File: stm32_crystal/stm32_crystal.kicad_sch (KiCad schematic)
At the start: 22 parts, among them U1 STM32F103C6Tx, U2 CR2032-BS-5-1, Y1 Crystal_Small, Y2 8Mhz

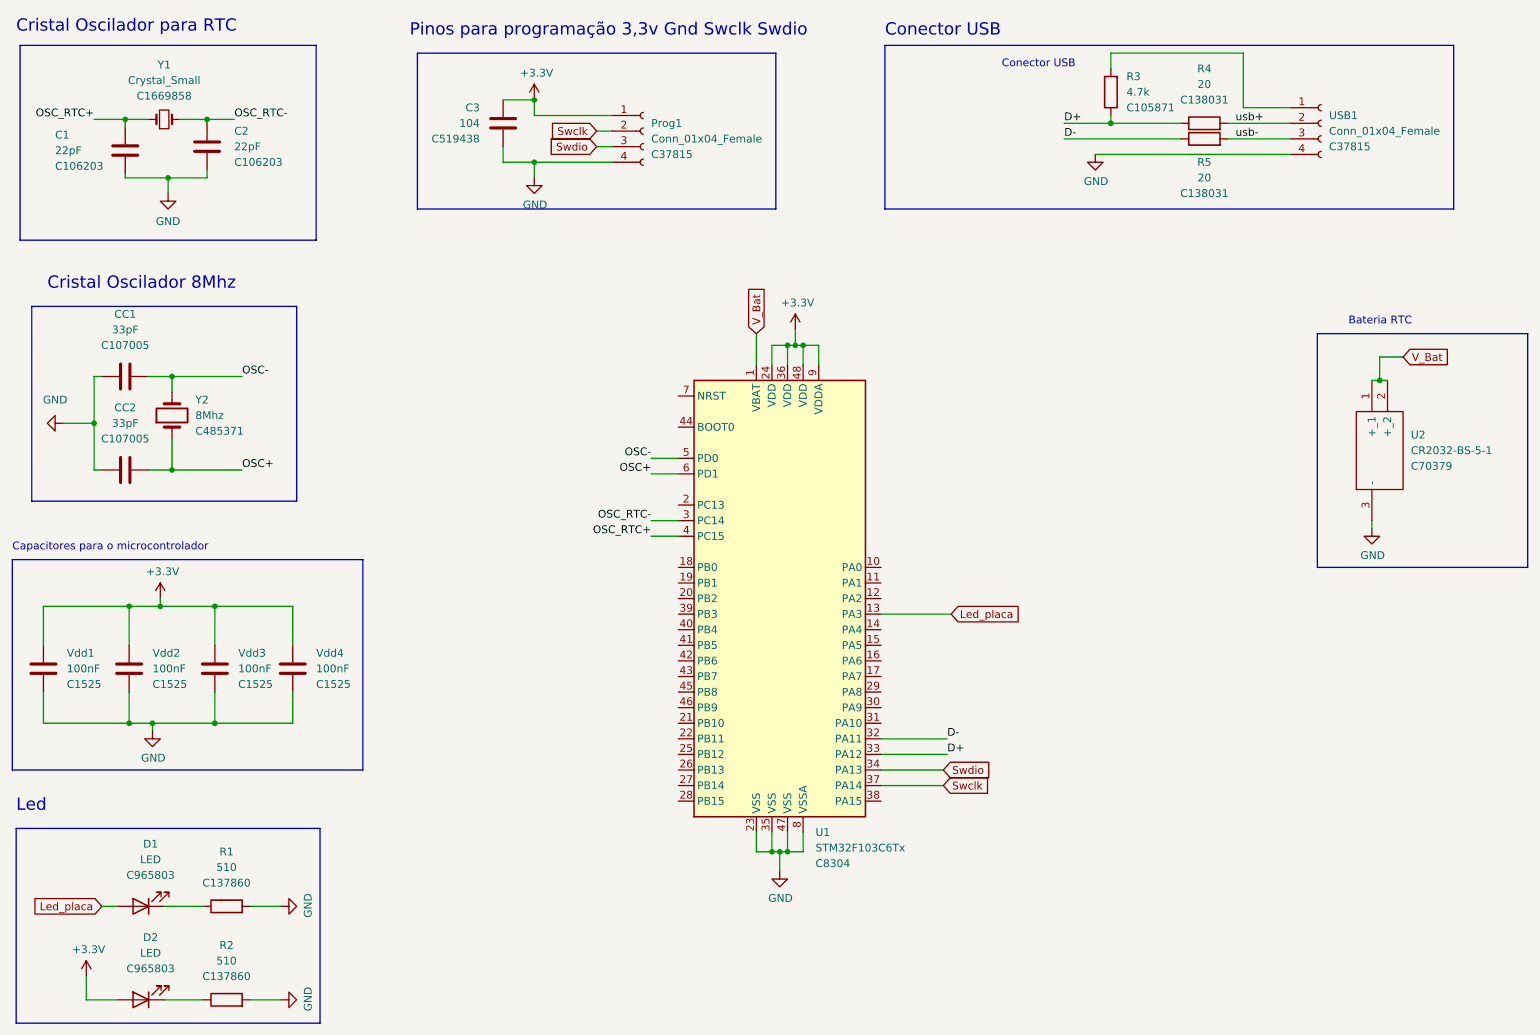
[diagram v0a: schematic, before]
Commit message: changes in stm and add can module
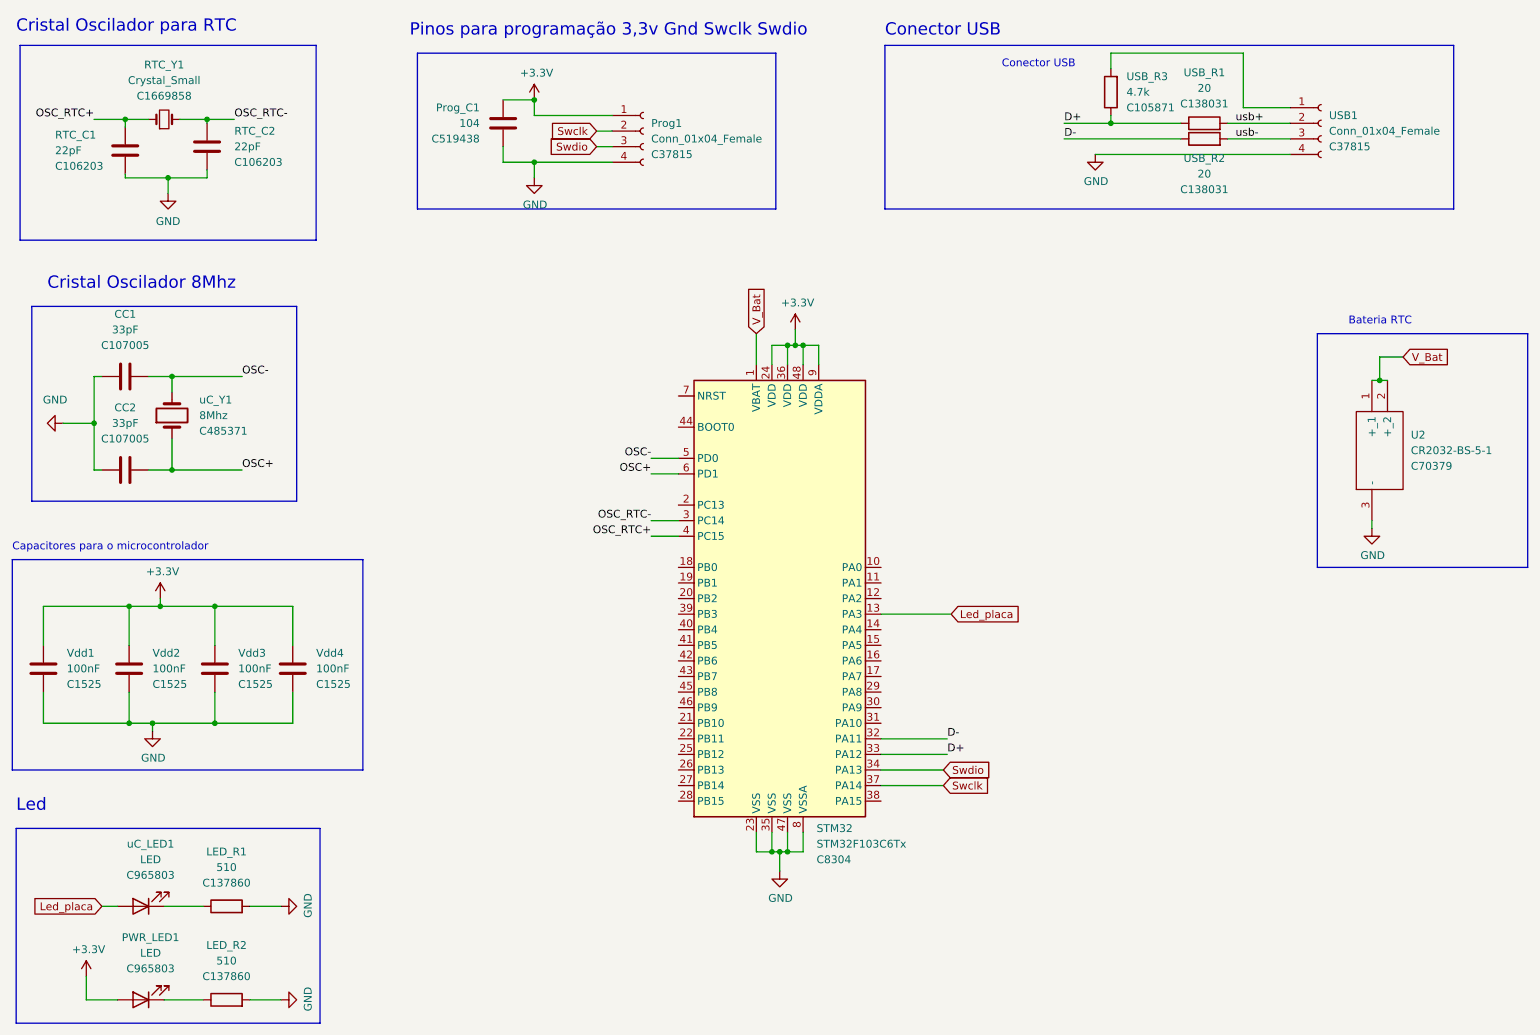
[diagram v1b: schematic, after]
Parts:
- renumbered R1 to LED_R1, R2 to LED_R2, D2 to PWR_LED1, C3 to Prog_C1, C1 to RTC_C1, C2 to RTC_C2, Y1 to RTC_Y1, U1 to STM32, R4 to USB_R1, R5 to USB_R2, R3 to USB_R3, D1 to uC_LED1, Y2 to uC_Y1
